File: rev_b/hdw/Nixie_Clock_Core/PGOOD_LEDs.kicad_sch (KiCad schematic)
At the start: 21 parts, among them U1601 74LVC1G97, U1602 74LVC1G97, U1603 74LVC1G97, U1604 74LVC1G97, U1605 74LVC1G97

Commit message: lots of rev B control board schematic progress
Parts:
- removed C1603: 0.1uF, Capacitors_SMD:C_0402, symbol Custom_Library:C_Custom
- removed D1603: Green, LEDs:LED_0402, symbol Device:LED
- removed R1604: 1k, Resistors_SMD:R_0402, symbol Custom_Library:R_Custom
- removed U1603: 74LVC1G97, Package_TO_SOT_SMD:SOT-363_SC-70-6, symbol Custom_Library:74LVC1G97_Power_NAND_INV
- renumbered C1602 to C?, C1604 to C?, C1605 to C?, C1601 to C?, D1604 to D?, D1601 to D?, D1605 to D?, D1602 to D?, R1605 to R?, R1602 to R?, R1601 to R?, R1606 to R?, R1603 to R?, U1605 to U?, U1602 to U?, U1601 to U?, U1604 to U?

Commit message: more carrier board progress
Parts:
- added C?: 0.1uF, Capacitors_SMD:C_0402, symbol Custom_Library:C_Custom
- added D?: Green, LEDs:LED_0402, symbol Device:LED
- added R?: 1k, Resistors_SMD:R_0402, symbol Custom_Library:R_Custom
- added U?: 74LVC1G97, Package_TO_SOT_SMD:SOT-363_SC-70-6, symbol Custom_Library:74LVC1G97_Power_NAND_INV
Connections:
- net +3.3V: now also C?.1, R?.1, U?.1 (VCC), U?.5 (VCC)
- net GND: now also C?.2, U?.2 (GND)
- net PGOOD_LED_SHDN: now also U?.3
- net POS12_PGOOD renamed POS24_PGOOD
- net POS5_PGOOD renamed POS180_PGOOD
- new net: D?.1 (K), U?.4
- new net: D?.2 (A), R?.2
- new net POS90_PGOOD: U?.6
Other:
- moved on the sheet: C?, D?, R?, U?

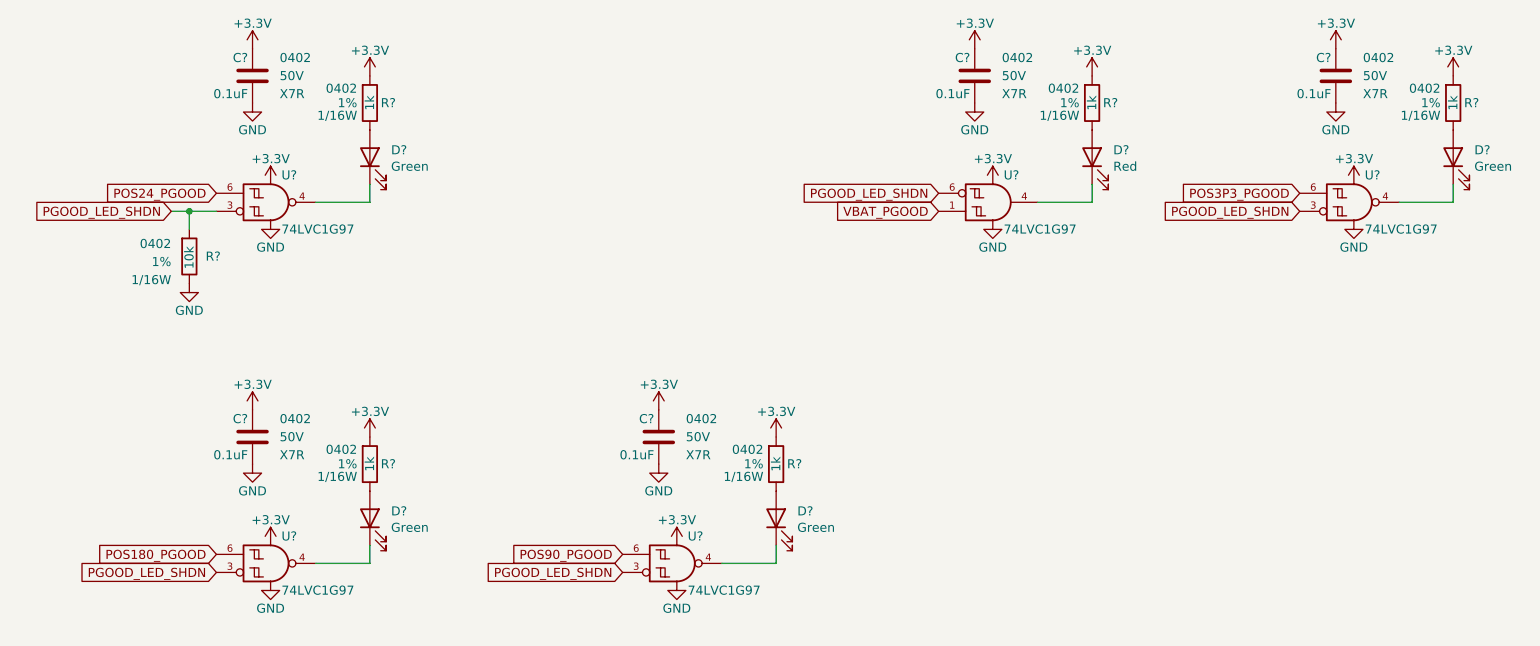
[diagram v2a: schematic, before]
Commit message: more schematic progress, assigning signals to MCU"
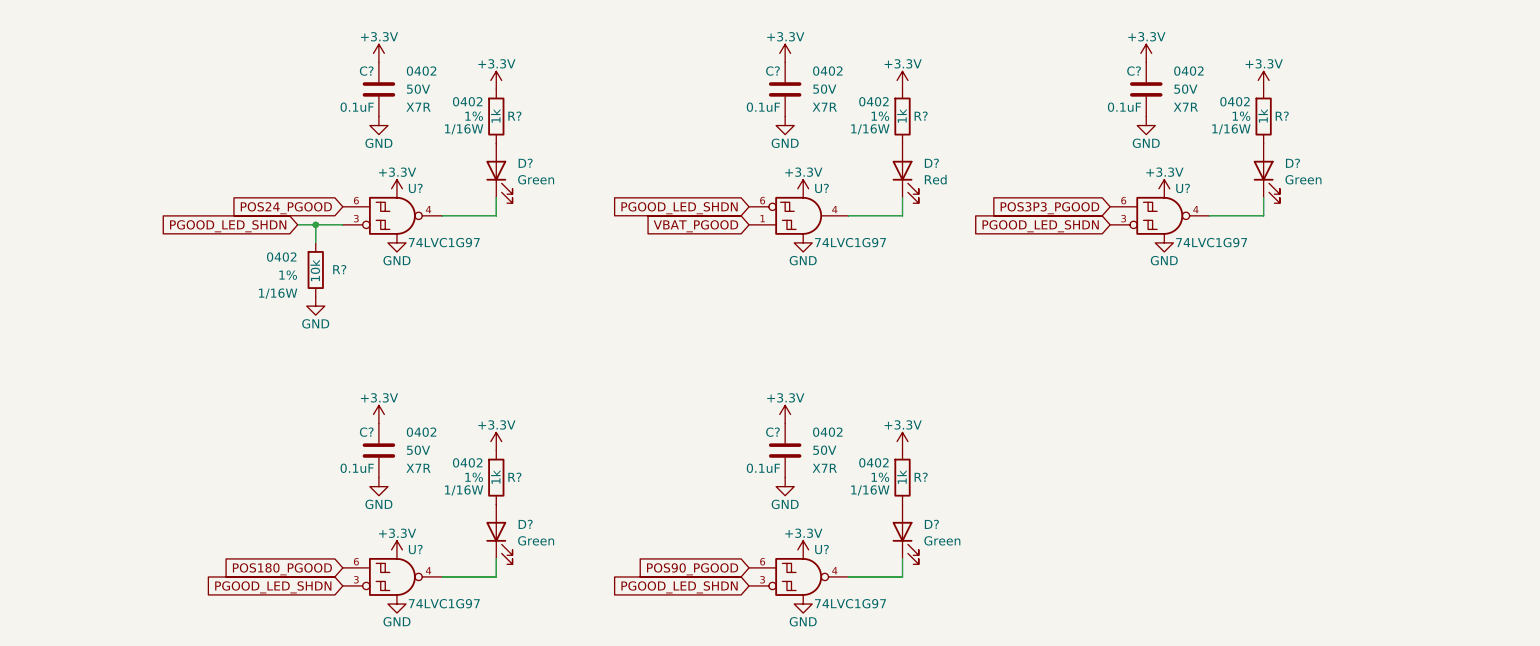
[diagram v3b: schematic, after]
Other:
- moved on the sheet: C?, D?, R?, U?

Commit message: updated footprints, ran some DRC
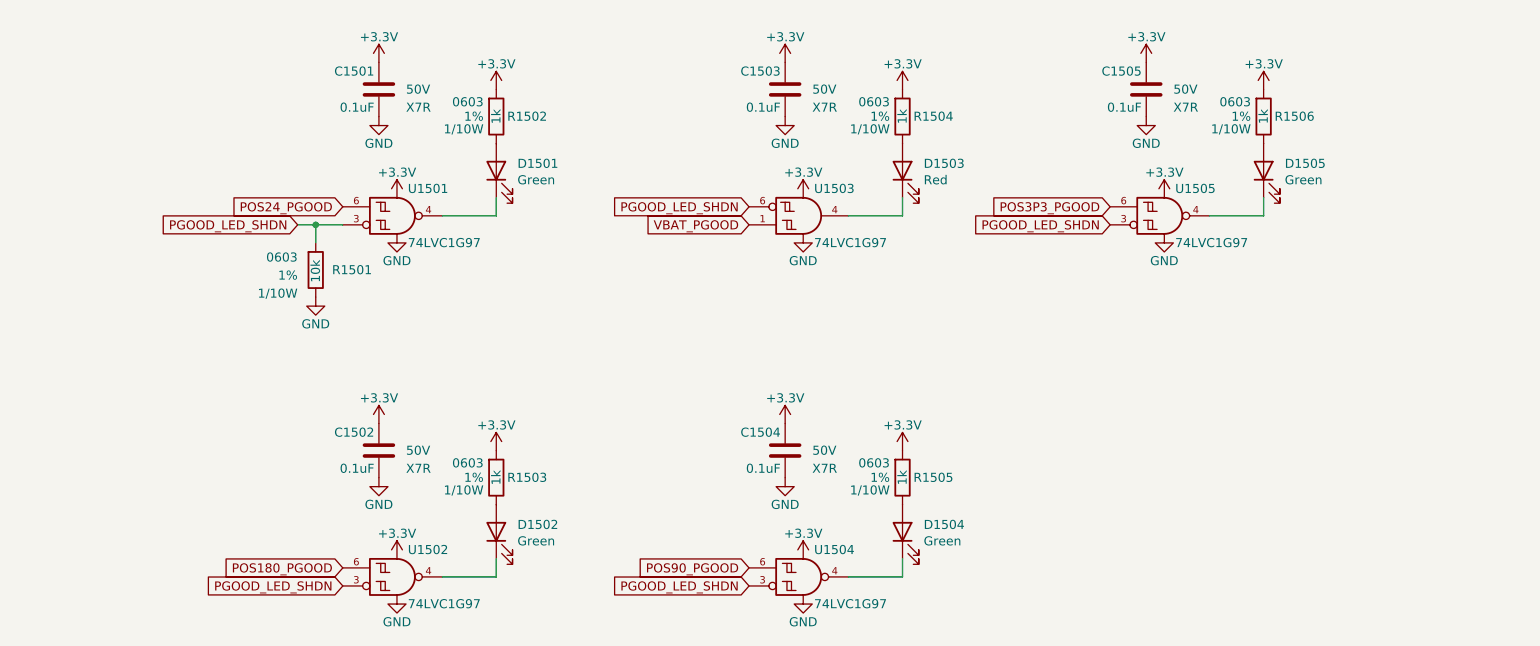
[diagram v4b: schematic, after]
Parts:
- C1501, C1502, C1503, C1504, C1505: renamed from C?; footprint Capacitors_SMD:C_0402 -> Capacitors_SMD:C_0603; Digi-Key PN 490-10698-1-ND -> (none); display_footprint 0402 -> (none)
- D1501, D1502, D1504, D1505: renamed from D?; footprint LEDs:LED_0402 -> LEDs:LED_0603; Digi-Key PN 1497-1219-1-ND -> 754-1121-1-ND
- D1503: renamed from D?; footprint LEDs:LED_0402 -> LEDs:LED_0603; Digi-Key PN 1497-1174-1-ND -> 754-1117-1-ND
- R1501: renamed from R?; footprint Resistors_SMD:R_0402 -> Resistors_SMD:R_0603; Digi-Key PN RMCF0402FT10K0CT-ND -> (none); Wattage 1/16W -> 1/10W; display_footprint 0402 -> 0603
- R1502, R1503, R1504, R1505, R1506: renamed from R?; footprint Resistors_SMD:R_0402 -> Resistors_SMD:R_0603; Digi-Key PN RMCF0402FT1K00CT-ND -> (none); Wattage 1/16W -> 1/10W; display_footprint 0402 -> 0603
- gave numbers to parts that had none: 5

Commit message: hid all passive refdes on core PCB
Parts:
- C1501, C1502, C1503, C1504, C1505: Digi-Key PN (none) -> 1276-1935-1-ND; display_footprint (none) -> 0603
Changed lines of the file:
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@@
       (effects (font (size 1.27 1.27)) hide)
     )
-    (property "Digi-Key PN" "" (at 70.485 97.155 0)
+    (property "Digi-Key PN" "1276-1935-1-ND" (at 70.485 97.155 0)
       (effects (font (size 1.524 1.524)) hide)
     )
-    (property "display_footprint" "" (at 85.09 107.315 0)
+    (property "display_footprint" "0603" (at 85.09 107.315 0)
       (effects (font (size 1.27 1.27)) (justify right))
     )
@@
       (effects (font (size 1.27 1.27)) hide)
     )
-    (property "Digi-Key PN" "" (at 127.635 46.355 0)
+    (property "Digi-Key PN" "1276-1935-1-ND" (at 127.635 46.355 0)
       (effects (font (size 1.524 1.524)) hide)
     )
-    (property "display_footprint" "" (at 142.24 56.515 0)
+    (property "display_footprint" "0603" (at 142.24 56.515 0)
       (effects (font (size 1.27 1.27)) (justify right))
     )
@@
       (effects (font (size 1.27 1.27)) hide)
     )
-    (property "Digi-Key PN" "" (at 178.435 46.355 0)
+    (property "Digi-Key PN" "1276-1935-1-ND" (at 178.435 46.355 0)
       (effects (font (size 1.524 1.524)) hide)
     )
-    (property "display_footprint" "" (at 193.04 56.515 0)
+    (property "display_footprint" "0603" (at 193.04 56.515 0)
       (effects (font (size 1.27 1.27)) (justify right))
     )
@@
       (effects (font (size 1.27 1.27)) hide)
     )
-    (property "Digi-Key PN" "" (at 70.485 46.355 0)
+    (property "Digi-Key PN" "1276-1935-1-ND" (at 70.485 46.355 0)
       (effects (font (size 1.524 1.524)) hide)
     )
-    (property "display_footprint" "" (at 85.09 56.515 0)
+    (property "display_footprint" "0603" (at 85.09 56.515 0)
       (effects (font (size 1.27 1.27)) (justify right))
     )
@@
       (effects (font (size 1.27 1.27)) hide)
     )
-    (property "Digi-Key PN" "" (at 127.635 97.155 0)
+    (property "Digi-Key PN" "1276-1935-1-ND" (at 127.635 97.155 0)
       (effects (font (size 1.524 1.524)) hide)
     )
-    (property "display_footprint" "" (at 142.24 107.315 0)
-      (effects (font (size 1.27 1.27)) (justify right))
-    )
+    (property "display_footprint" "0603" (at 142.24 107.315 0)
+      (effects (font (size 1.27 1.27)) (justify right))
+    )

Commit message: added BOM
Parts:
- R1501: Digi-Key PN (none) -> 541-10.0KHCT-ND
- R1502, R1503, R1504, R1505, R1506: Digi-Key PN (none) -> 541-1.00KHCT-ND
- U1501, U1502, U1503, U1504, U1505: Digi-Key PN 1727-1772-1-ND -> 296-15582-1-ND
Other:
- title: (none) -> Nixie Clock Redux Core Board
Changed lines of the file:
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@@
   (paper "A")
   (title_block
-    (date "2023-05-12")
-    (rev "PRELIM")
+    (title "Nixie Clock Redux Core Board")
+    (date "2023-07-30")
+    (rev "B")
     (company "Drew Maatman")
   )
@@
     (stroke (width 0) (type default))
   )
-  (global_label "POS24_PGOOD" (shape input) (at 76.2 75.565 180)
+  (global_label "POS24_PGOOD" (shape input) (at 76.2 75.565 180) (fields_autoplaced)
     (effects (font (size 1.27 1.27)) (justify right))
-    (property "Intersheetrefs" "${INTERSHEET_REFS}" (at 76.2 75.565 0)
-      (effects (font (size 1.27 1.27)) hide)
-    )
-  )
-  (global_label "PGOOD_LED_SHDN" (shape input) (at 69.85 78.105 180)
+    (property "Intersheetrefs" "${INTERSHEET_REFS}" (at 59.6266 75.565 0)
+      (effects (font (size 1.27 1.27)) (justify right))
+    )
+  )
+  (global_label "PGOOD_LED_SHDN" (shape input) (at 69.85 78.105 180) (fields_autoplaced)
     (effects (font (size 1.27 1.27)) (justify right))
-    (property "Intersheetrefs" "${INTERSHEET_REFS}" (at 69.85 78.105 0)
-      (effects (font (size 1.27 1.27)) hide)
-    )
-  )
-  (global_label "PGOOD_LED_SHDN" (shape input) (at 184.15 78.105 180)
+    (property "Intersheetrefs" "${INTERSHEET_REFS}" (at 49.9504 78.105 0)
+      (effects (font (size 1.27 1.27)) (justify right))
+    )
+  )
+  (global_label "PGOOD_LED_SHDN" (shape input) (at 184.15 78.105 180) (fields_autoplaced)
     (effects (font (size 1.27 1.27)) (justify right))
-    (property "Intersheetrefs" "${INTERSHEET_REFS}" (at 184.15 78.105 0)
-      (effects (font (size 1.27 1.27)) hide)
-    )
-  )
-  (global_label "POS180_PGOOD" (shape input) (at 76.2 126.365 180)
+    (property "Intersheetrefs" "${INTERSHEET_REFS}" (at 164.2504 78.105 0)
+      (effects (font (size 1.27 1.27)) (justify right))
+    )
+  )
+  (global_label "POS180_PGOOD" (shape input) (at 76.2 126.365 180) (fields_autoplaced)
     (effects (font (size 1.27 1.27)) (justify right))
-    (property "Intersheetrefs" "${INTERSHEET_REFS}" (at 76.2 126.365 0)
-      (effects (font (size 1.27 1.27)) hide)
-    )
-  )
-  (global_label "PGOOD_LED_SHDN" (shape input) (at 76.2 128.905 180)
+    (property "Intersheetrefs" "${INTERSHEET_REFS}" (at 58.4171 126.365 0)
+      (effects (font (size 1.27 1.27)) (justify right))
+    )
+  )
+  (global_label "PGOOD_LED_SHDN" (shape input) (at 76.2 128.905 180) (fields_autoplaced)
     (effects (font (size 1.27 1.27)) (justify right))
-    (property "Intersheetrefs" "${INTERSHEET_REFS}" (at 76.2 128.905 0)
-      (effects (font (size 1.27 1.27)) hide)
-    )
-  )
-  (global_label "POS3P3_PGOOD" (shape input) (at 184.15 75.565 180)
+    (property "Intersheetrefs" "${INTERSHEET_REFS}" (at 56.3004 128.905 0)
+      (effects (font (size 1.27 1.27)) (justify right))
+    )
+  )
+  (global_label "POS3P3_PGOOD" (shape input) (at 184.15 75.565 180) (fields_autoplaced)
     (effects (font (size 1.27 1.27)) (justify right))
-    (property "Intersheetrefs" "${INTERSHEET_REFS}" (at 184.15 75.565 0)
-      (effects (font (size 1.27 1.27)) hide)
-    )
-  )
-  (global_label "POS90_PGOOD" (shape input) (at 133.35 126.365 180)
+    (property "Intersheetrefs" "${INTERSHEET_REFS}" (at 166.3066 75.565 0)
+      (effects (font (size 1.27 1.27)) (justify right))
+    )
+  )
+  (global_label "POS90_PGOOD" (shape input) (at 133.35 126.365 180) (fields_autoplaced)
     (effects (font (size 1.27 1.27)) (justify right))
-    (property "Intersheetrefs" "${INTERSHEET_REFS}" (at 133.35 126.365 0)
-      (effects (font (size 1.27 1.27)) hide)
-    )
-  )
-  (global_label "VBAT_PGOOD" (shape input) (at 133.35 78.105 180)
+    (property "Intersheetrefs" "${INTERSHEET_REFS}" (at 116.7766 126.365 0)
+      (effects (font (size 1.27 1.27)) (justify right))
+    )
+  )
+  (global_label "VBAT_PGOOD" (shape input) (at 133.35 78.105 180) (fields_autoplaced)
     (effects (font (size 1.27 1.27)) (justify right))
-    (property "Intersheetrefs" "${INTERSHEET_REFS}" (at 133.35 78.105 0)
-      (effects (font (size 1.27 1.27)) hide)
-    )
-  )
-  (global_label "PGOOD_LED_SHDN" (shape input) (at 133.35 75.565 180)
+    (property "Intersheetrefs" "${INTERSHEET_REFS}" (at 118.5908 78.105 0)
+      (effects (font (size 1.27 1.27)) (justify right))
+    )
+  )
+  (global_label "PGOOD_LED_SHDN" (shape input) (at 133.35 75.565 180) (fields_autoplaced)
     (effects (font (size 1.27 1.27)) (justify right))
-    (property "Intersheetrefs" "${INTERSHEET_REFS}" (at 133.35 75.565 0)
-      (effects (font (size 1.27 1.27)) hide)
-    )
-  )
-  (global_label "PGOOD_LED_SHDN" (shape input) (at 133.35 128.905 180)
+    (property "Intersheetrefs" "${INTERSHEET_REFS}" (at 113.4504 75.565 0)
+      (effects (font (size 1.27 1.27)) (justify right))
+    )
+  )
+  (global_label "PGOOD_LED_SHDN" (shape input) (at 133.35 128.905 180) (fields_autoplaced)
     (effects (font (size 1.27 1.27)) (justify right))
-    (property "Intersheetrefs" "${INTERSHEET_REFS}" (at 133.35 128.905 0)
-      (effects (font (size 1.27 1.27)) hide)
+    (property "Intersheetrefs" "${INTERSHEET_REFS}" (at 113.4504 128.905 0)
+      (effects (font (size 1.27 1.27)) (justify right))
     )
   )
@@
       (effects (font (size 1.27 1.27)) (justify left))
     )
-    (property "Digi-Key PN" "" (at 147.32 52.705 0)
+    (property "Digi-Key PN" "541-1.00KHCT-ND" (at 147.32 52.705 0)
       (effects (font (size 1.524 1.524)) hide)
     )
@@
       (effects (font (size 1.27 1.27)) hide)
     )
-    (property "Digi-Key PN" "1727-1772-1-ND" (at 191.77 76.835 0)
+    (property "Digi-Key PN" "296-15582-1-ND" (at 191.77 76.835 0)
       (effects (font (size 1.27 1.27)) hide)
     )
@@
       (effects (font (size 1.27 1.27)) hide)
     )
-    (property "Digi-Key PN" "1727-1772-1-ND" (at 140.97 127.635 0)
+    (property "Digi-Key PN" "296-15582-1-ND" (at 140.97 127.635 0)
       (effects (font (size 1.27 1.27)) hide)
     )
@@
       (effects (font (size 1.27 1.27)) (justify left))
     )
-    (property "Digi-Key PN" "" (at 90.17 52.705 0)
+    (property "Digi-Key PN" "541-1.00KHCT-ND" (at 90.17 52.705 0)
       (effects (font (size 1.524 1.524)) hide)
     )
@@
       (effects (font (size 1.27 1.27)) (justify left))
     )
-    (property "Digi-Key PN" "" (at 64.77 74.295 0)
+    (property "Digi-Key PN" "541-10.0KHCT-ND" (at 64.77 74.295 0)
       (effects (font (size 1.524 1.524)) hide)
     )
@@
       (effects (font (size 1.27 1.27)) (justify left))
     )
-    (property "Digi-Key PN" "" (at 198.12 52.705 0)
+    (property "Digi-Key PN" "541-1.00KHCT-ND" (at 198.12 52.705 0)
       (effects (font (size 1.524 1.524)) hide)
     )
@@
       (effects (font (size 1.27 1.27)) hide)
     )
-    (property "Digi-Key PN" "1727-1772-1-ND" (at 83.82 127.635 0)
+    (property "Digi-Key PN" "296-15582-1-ND" (at 83.82 127.635 0)
       (effects (font (size 1.27 1.27)) hide)
     )
@@
       (effects (font (size 1.27 1.27)) (justify left))
     )
-    (property "Digi-Key PN" "" (at 90.17 103.505 0)
+    (property "Digi-Key PN" "541-1.00KHCT-ND" (at 90.17 103.505 0)
       (effects (font (size 1.524 1.524)) hide)
     )
@@
       (effects (font (size 1.27 1.27)) hide)
     )
-    (property "Digi-Key PN" "1727-1772-1-ND" (at 83.82 76.835 0)
+    (property "Digi-Key PN" "296-15582-1-ND" (at 83.82 76.835 0)
       (effects (font (size 1.27 1.27)) hide)
     )
@@
       (effects (font (size 1.27 1.27)) hide)
     )
-    (property "Digi-Key PN" "1727-1772-1-ND" (at 140.97 76.835 0)
+    (property "Digi-Key PN" "296-15582-1-ND" (at 140.97 76.835 0)
       (effects (font (size 1.27 1.27)) hide)
     )
@@
       (effects (font (size 1.27 1.27)) (justify left))
     )
-    (property "Digi-Key PN" "" (at 147.32 103.505 0)
+    (property "Digi-Key PN" "541-1.00KHCT-ND" (at 147.32 103.505 0)
       (effects (font (size 1.524 1.524)) hide)
     )
